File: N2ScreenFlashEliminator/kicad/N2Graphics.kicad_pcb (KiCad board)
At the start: 2 copper layers, 51 x 38 mm, 14 parts, among them J1 Header, Q1 BC557, SW1 Cap Enable, SW2 Unit Enable, U1 74LS00, U2 74LS74, U3 74LS32

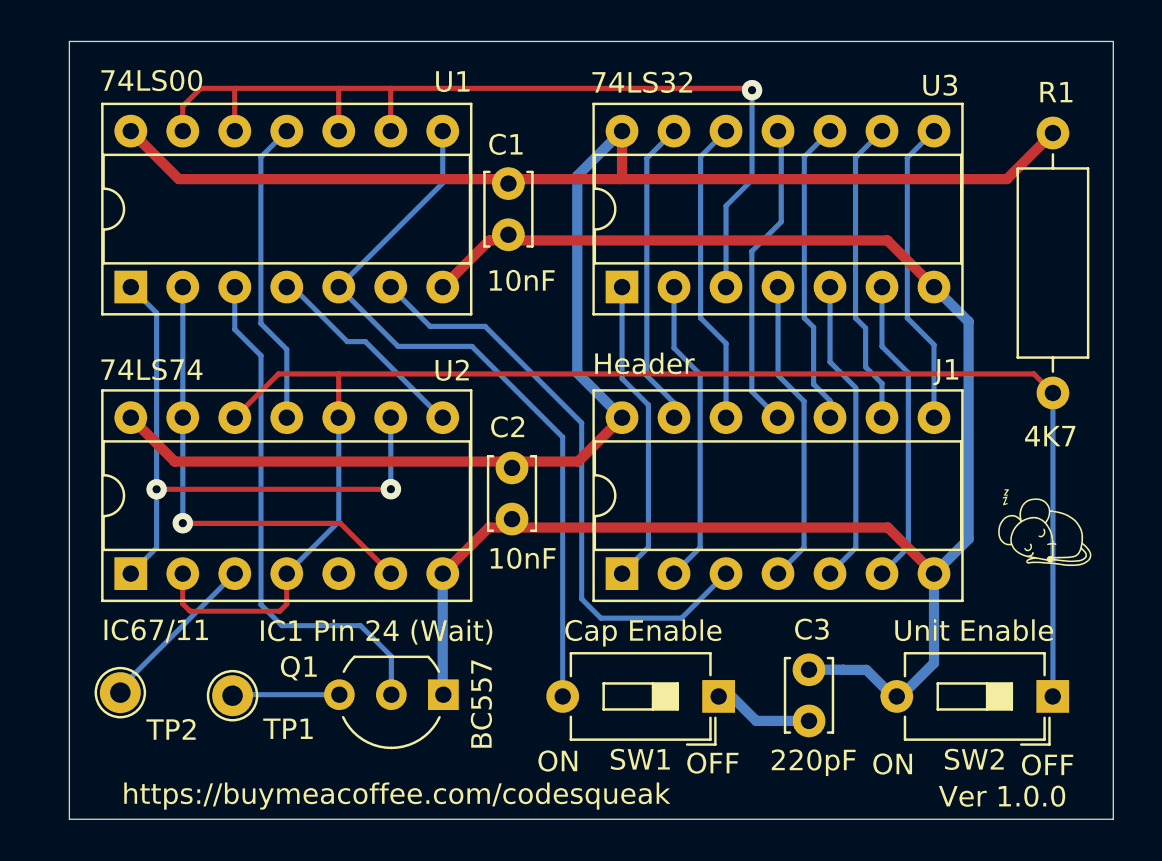
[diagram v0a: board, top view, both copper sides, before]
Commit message: Flip enable switch position
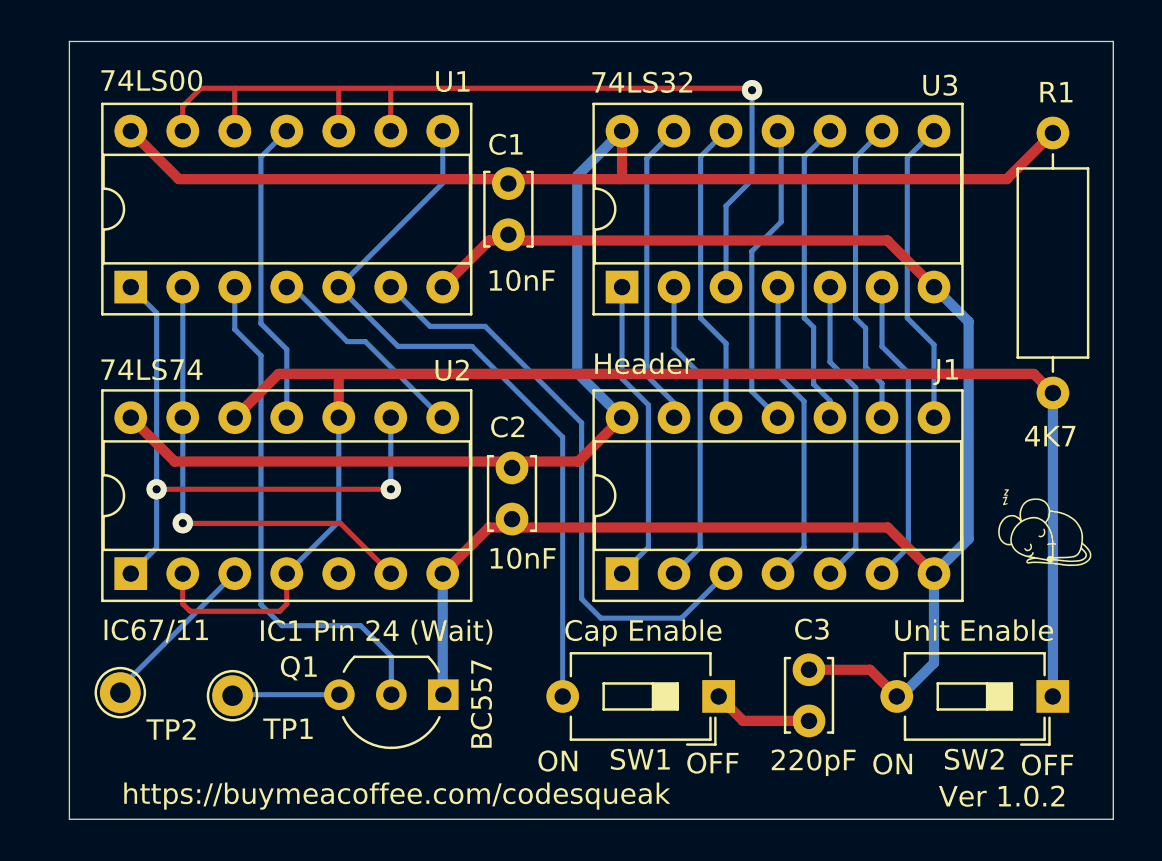
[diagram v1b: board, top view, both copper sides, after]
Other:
- board text added: "CS-001"
- board text added: "Ver 1.0.2"
- board text removed: "Ver 1.0.0"
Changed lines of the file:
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@@
       (drillshape 0)
       (scaleselection 1)
-      (outputdirectory "pcbway//")
+      (outputdirectory "jlcpcb/")
     )
   )
@@
   (gr_line (start 109 82) (end 160 82)
     (stroke (width 0.05) (type solid)) (layer "Edge.Cuts"))
+  (gr_text "CS-001" (at 119.820064 80.597686) (layer "B.SilkS")
+    (effects (font (size 1.5 1.5) (thickness 0.3) bold) (justify left bottom mirror))
+  )
   (gr_text "buymeacoffee is  a website that connects developers, \n\n    designers, artists etc with     their communities so\n      that people can express     appreciation.\nIf you would like to contribute    ,feel free to\n\n\n   do it at Buy me a coffee!,\n   (https://www.buymeacoffee.com/codesqueak)\n\n\n  and many thanks in advance\n" (at 155.669604 64.975441) (layer "B.SilkS")
     (effects (font (size 1 1) (thickness 0.15)) (justify left bottom mirror))
@@
     (effects (font (size 1 1) (thickness 0.15)) (justify left bottom))
   )
-  (gr_text "Ver 1.0.0" (at 151.469318 81.494777) (layer "F.SilkS")
+  (gr_text "Ver 1.0.2" (at 151.469318 81.494777) (layer "F.SilkS")
     (effects (font (size 1 1) (thickness 0.15)) (justify left bottom))
   )
-  (segment (start 145.133336 77.194891) (end 142.55472 77.194891) (width 0.5) (layer "B.Cu") (net 1))
-  (segment (start 142.55472 77.194891) (end 141.029814 75.669985) (width 0.5) (layer "B.Cu") (net 1))
+  (segment (start 145.133336 77.194891) (end 141.914685 77.194891) (width 0.5) (layer "F.Cu") (net 1))
+  (segment (start 141.914685 77.194891) (end 140.719794 76) (width 0.5) (layer "F.Cu") (net 1))
   (segment (start 136 70) (end 137.288579 68.711421) (width 0.25) (layer "B.Cu") (net 2))
   (segment (start 137.288579 61.760726) (end 136 60.472147) (width 0.25) (layer "B.Cu") (net 2))
@@
   (segment (start 151.24 70) (end 148.987343 67.747343) (width 0.5) (layer "F.Cu") (net 9))
   (segment (start 129.519589 53.720411) (end 127.24 56) (width 0.5) (layer "F.Cu") (net 9))
+  (segment (start 148.117021 74.694891) (end 149.42213 76) (width 0.5) (layer "F.Cu") (net 9))
   (segment (start 129.492657 67.747343) (end 127.24 70) (width 0.5) (layer "F.Cu") (net 9))
+  (segment (start 145.133336 74.694891) (end 148.117021 74.694891) (width 0.5) (layer "F.Cu") (net 9))
   (segment (start 151.24 56) (end 148.960411 53.720411) (width 0.5) (layer "F.Cu") (net 9))
   (segment (start 148.960411 53.720411) (end 129.519589 53.720411) (width 0.5) (layer "F.Cu") (net 9))
@@
   (segment (start 152.93184 68.30816) (end 151.24 70) (width 0.5) (layer "B.Cu") (net 9))
   (segment (start 151.24 56) (end 152.93184 57.69184) (width 0.5) (layer "B.Cu") (net 9))
-  (segment (start 149.42213 76.185931) (end 147.936809 74.70061) (width 0.5) (layer "B.Cu") (net 9))
   (segment (start 127.24 70) (end 127.24 75.885254) (width 0.5) (layer "B.Cu") (net 9))
-  (segment (start 146.80582 74.694891) (end 145.133336 74.694891) (width 0.5) (layer "B.Cu") (net 9))
-  (segment (start 147.936809 74.70061) (end 146.811539 74.70061) (width 0.5) (layer "B.Cu") (net 9))
   (segment (start 151.24 74.368061) (end 149.42213 76.185931) (width 0.5) (layer "B.Cu") (net 9))
   (segment (start 151.24 70) (end 151.24 74.368061) (width 0.5) (layer "B.Cu") (net 9))
-  (segment (start 146.811539 74.70061) (end 146.80582 74.694891) (width 0.5) (layer "B.Cu") (net 9))
   (segment (start 149.934303 49.685697) (end 151.24 48.38) (width 0.25) (layer "B.Cu") (net 10))
   (segment (start 151.24 58.819701) (end 149.934303 57.514004) (width 0.25) (layer "B.Cu") (net 10))
@@
   (segment (start 122.188962 75.914216) (end 117.0204 75.914216) (width 0.25) (layer "B.Cu") (net 17))
   (segment (start 119.278172 71.833913) (end 114.893303 71.833913) (width 0.25) (layer "F.Cu") (net 18))
-  (segment (start 122.152626 60.24213) (end 156.118725 60.24213) (width 0.25) (layer "F.Cu") (net 18))
-  (segment (start 122.152626 60.24213) (end 119.21787 60.24213) (width 0.25) (layer "F.Cu") (net 18))
+  (segment (start 122.152626 60.24213) (end 156.118725 60.24213) (width 0.5) (layer "F.Cu") (net 18))
+  (segment (start 122.152626 60.24213) (end 119.21787 60.24213) (width 0.5) (layer "F.Cu") (net 18))
   (segment (start 122.16 60.249504) (end 122.152626 60.24213) (width 0.25) (layer "F.Cu") (net 18))
   (segment (start 119.62 71.492085) (end 119.278172 71.833913) (width 0.25) (layer "F.Cu") (net 18))
   (segment (start 119.62 70) (end 119.62 71.492085) (width 0.25) (layer "F.Cu") (net 18))
-  (segment (start 122.16 62.38) (end 122.16 60.249504) (width 0.25) (layer "F.Cu") (net 18))
-  (segment (start 157.050096 61.173501) (end 156.118725 60.24213) (width 0.25) (layer "F.Cu") (net 18))
+  (segment (start 122.16 62.38) (end 122.16 60.249504) (width 0.5) (layer "F.Cu") (net 18))
+  (segment (start 157.050096 61.173501) (end 156.118725 60.24213) (width 0.5) (layer "F.Cu") (net 18))
   (segment (start 114.54 71.48061) (end 114.54 70) (width 0.25) (layer "F.Cu") (net 18))
-  (segment (start 119.21787 60.24213) (end 117.08 62.38) (width 0.25) (layer "F.Cu") (net 18))
+  (segment (start 119.21787 60.24213) (end 117.08 62.38) (width 0.5) (layer "F.Cu") (net 18))
   (segment (start 114.893303 71.833913) (end 114.54 71.48061) (width 0.25) (layer "F.Cu") (net 18))
   (segment (start 122.16 67.46) (end 119.62 70) (width 0.25) (layer "B.Cu") (net 18))
-  (segment (start 157.050096 61.173501) (end 157.050096 76.177965) (width 0.25) (layer "B.Cu") (net 18))
+  (segment (start 157.050096 61.173501) (end 157.050096 76.177965) (width 0.5) (layer "B.Cu") (net 18))
   (segment (start 122.16 62.38) (end 122.16 67.46) (width 0.25) (layer "B.Cu") (net 18))
   (segment (start 122.16 56) (end 125.05807 58.89807) (width 0.25) (layer "B.Cu") (net 19))

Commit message: Kicad 9 updates
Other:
- board text added: "8a0fbfad-baae-4ae9-97e5-829d795d34c3"
- board text added: "Ver 1.1"
- board text removed: "22e31ff8-705e-4c1f-9c94-7f2cd4717822"
- board text removed: "Ver 1.0.2"

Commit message: Minor changes
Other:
- board text added: "41ec1422-d5ef-4889-9045-bffbed790e82"
- board text added: "CS-008"
- board text removed: "8a0fbfad-baae-4ae9-97e5-829d795d34c3"
- board text removed: "CS-001"
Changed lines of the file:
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@@
 		)
 	)
-	(gr_text "CS-001"
+	(gr_text "CS-008"
 		(at 119.820064 80.597686 0)
 		(layer "B.SilkS")
@@
 		)
 	)
-	(gr_text "8a0fbfad-baae-4ae9-97e5-829d795d34c3"
+	(gr_text "41ec1422-d5ef-4889-9045-bffbed790e82"
 		(at 157.490581 80.593881 0)
 		(layer "B.SilkS")
